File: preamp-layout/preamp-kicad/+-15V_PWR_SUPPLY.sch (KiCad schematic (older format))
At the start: 33 parts, among them J10 Conn_01x03_Male, J11 Conn_01x03_Male, J8 Screw_Terminal_01x03, J9 Conn_01x03_Male, T1 Transformer_1P_2S, U1 LM7815, U2 LM7915

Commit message: Power Supply Update
Grounding made more clear, tied to chassis on AC board. Pins renamed. Aligned with AC wall power convention. General cleanup.
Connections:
- net labels added: AC_HOT, AC_N
- net labels removed: AC+, AC-
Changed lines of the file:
@@
 $EndDescr
 Text HLabel 1950 3250 1    50   UnSpc ~ 0
-AC+
+AC_HOT
 Text HLabel 1950 3650 3    50   UnSpc ~ 0
-AC-
+AC_N
 Text GLabel 3900 6000 1    50   UnSpc ~ 0
 +15V

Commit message: RefDes Update
Re-ran refdes assignment, updated BOM accordingly.
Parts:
- renumbered J11 to J10, J8 to J7, J9 to J8, J10 to J9
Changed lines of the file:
@@
 	4150 3450 4150 4050
 $Comp
-L Connector:Conn_01x03_Male J9
+L Connector:Conn_01x03_Male J8
 U 1 1 5E5A9FCF
 P 3100 5800
-AR Path="/5E27B612/5E5A9FCF" Ref="J9"  Part="1"
+AR Path="/5E27B612/5E5A9FCF" Ref="J8"  Part="1"
 AR Path="/6009D432/5E5A9FCF" Ref="J?"  Part="1"
 AR Path="/5E1A0CE1/5E5A9FCF" Ref="J?"  Part="1"
-F 0 "J9" H 3072 5778 50  0000 R CNN
+F 0 "J8" H 3072 5778 50  0000 R CNN
 F 1 "Conn_01x03_Male" H 3072 5733 50  0001 R CNN
 F 2 "Connector_JST:JST_EH_B3B-EH-A_1x03_P2.50mm_Vertical" H 3100 5800 50  0001 C CNN
@@
 $EndComp
 $Comp
-L Connector:Conn_01x03_Male J10
+L Connector:Conn_01x03_Male J9
 U 1 1 5E5BC88E
 P 3100 6400
-AR Path="/5E27B612/5E5BC88E" Ref="J10"  Part="1"
+AR Path="/5E27B612/5E5BC88E" Ref="J9"  Part="1"
 AR Path="/6009D432/5E5BC88E" Ref="J?"  Part="1"
 AR Path="/5E1A0CE1/5E5BC88E" Ref="J?"  Part="1"
-F 0 "J10" H 3072 6378 50  0000 R CNN
+F 0 "J9" H 3072 6378 50  0000 R CNN
 F 1 "Conn_01x03_Male" H 3072 6333 50  0001 R CNN
 F 2 "Connector_JST:JST_EH_B3B-EH-A_1x03_P2.50mm_Vertical" H 3100 6400 50  0001 C CNN
@@
 $EndComp
 $Comp
-L Connector:Conn_01x03_Male J11
+L Connector:Conn_01x03_Male J10
 U 1 1 5E5C1243
 P 3100 7000
-AR Path="/5E27B612/5E5C1243" Ref="J11"  Part="1"
+AR Path="/5E27B612/5E5C1243" Ref="J10"  Part="1"
 AR Path="/6009D432/5E5C1243" Ref="J?"  Part="1"
 AR Path="/5E1A0CE1/5E5C1243" Ref="J?"  Part="1"
-F 0 "J11" H 3072 6978 50  0000 R CNN
+F 0 "J10" H 3072 6978 50  0000 R CNN
 F 1 "Conn_01x03_Male" H 3072 6933 50  0001 R CNN
 F 2 "Connector_JST:JST_EH_B3B-EH-A_1x03_P2.50mm_Vertical" H 3100 7000 50  0001 C CNN
@@
 AR Path="/5E26F6FE/5E8FCAF8" Ref="J?"  Part="1"
 AR Path="/5E5EF2D4/5E8FCAF8" Ref="J?"  Part="1"
-AR Path="/5E27B612/5E8FCAF8" Ref="J8"  Part="1"
-F 0 "J8" H 1268 3675 50  0000 C CNN
+AR Path="/5E27B612/5E8FCAF8" Ref="J7"  Part="1"
+F 0 "J7" H 1268 3675 50  0000 C CNN
 F 1 "Screw_Terminal_01x03" H 1268 3216 50  0001 C CNN
 F 2 "TerminalBlock_Phoenix:TerminalBlock_Phoenix_MKDS-3-3-5.08_1x03_P5.08mm_Horizontal" H 1350 3450 50  0001 C CNN

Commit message: Prelim PCB layout
Work done to lay out PCBs. Saving in anticipation of creating branch with a different input switching topology.
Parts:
- removed RV1, RV2: 5k, symbol Device:R_POT_US
- removed U1: LM7815, Package_TO_SOT_THT:TO-220-3_Vertical, symbol Regulator_Linear:L7805
- removed U2: LM7915, Package_TO_SOT_THT:TO-220-3_Vertical, symbol Regulator_Linear:LM7905_TO220
- added RV1, RV2: 4.7k, Potentiometer_THT:Potentiometer_Bourns_3386P_Vertical, symbol Device:R_POT
- added U1: LM7815, Package_TO_SOT_THT:TO-220-3_Vertical, symbol Regulator_Linear:LM7815_TO220
- added U2: LM7915, Package_TO_SOT_THT:TO-220-3_Vertical, symbol Regulator_Linear:LM7915_TO220
- F2: footprint (none) -> preamp:01110501Z_3AG
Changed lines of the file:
@@
 F 0 "F2" V 2053 3350 50  0000 C CNN
 F 1 "500mA" V 2144 3350 50  0000 C CNN
-F 2 "" V 2180 3350 50  0001 C CNN
+F 2 "preamp:01110501Z_3AG" V 2180 3350 50  0001 C CNN
 F 3 "~" H 2250 3350 50  0001 C CNN
 	1    2250 3350
@@
 	1    0    0    -1
 $EndComp
-Text Label 3550 4050 3    50   ~ 0
+Text Label 3550 4000 3    50   ~ 0
 rectified_-
-Text Label 4150 4050 3    50   ~ 0
+Text Label 4150 4000 3    50   ~ 0
 rectified_+
 $Comp
@@
 Text Label 5500 2350 2    50   ~ 0
 rectified_+
-$Comp
-L Regulator_Linear:L7805 U?
-U 1 1 5FE3F8F2
-P 7800 2350
-AR Path="/5E5EF2D4/5FE3F8F2" Ref="U?"  Part="1"
-AR Path="/5E27B612/5FE3F8F2" Ref="U1"  Part="1"
-F 0 "U1" H 7800 2592 50  0000 C CNN
-F 1 "LM7815" H 7800 2501 50  0000 C CNN
-F 2 "Package_TO_SOT_THT:TO-220-3_Vertical" H 7825 2200 50  0001 L CIN
-F 3 "http://www.st.com/content/ccc/resource/technical/document/datasheet/41/4f/b3/b0/12/d4/47/88/CD00000444.pdf/files/CD00000444.pdf/jcr:content/translations/en.CD00000444.pdf" H 7800 2300 50  0001 C CNN
-	1    7800 2350
-	1    0    0    -1
-$EndComp
 Connection ~ 5700 3550
-$Comp
-L Regulator_Linear:LM7905_TO220 U?
-U 1 1 5FE3F8FA
-P 7800 4750
-AR Path="/5E5EF2D4/5FE3F8FA" Ref="U?"  Part="1"
-AR Path="/5E27B612/5FE3F8FA" Ref="U2"  Part="1"
-F 0 "U2" H 7800 4601 50  0000 C CNN
-F 1 "LM7915" H 7800 4510 50  0000 C CNN
-F 2 "Package_TO_SOT_THT:TO-220-3_Vertical" H 7800 4550 50  0001 C CIN
-F 3 "http://www.fairchildsemi.com/ds/LM/LM7905.pdf" H 7800 4750 50  0001 C CNN
-	1    7800 4750
-	1    0    0    -1
-$EndComp
-$Comp
-L Device:R_POT_US RV?
-U 1 1 5FE3F900
-P 7800 3250
-AR Path="/5E5EF2D4/5FE3F900" Ref="RV?"  Part="1"
-AR Path="/5E27B612/5FE3F900" Ref="RV1"  Part="1"
-F 0 "RV1" H 7732 3296 50  0000 R CNN
-F 1 "5k" H 7732 3205 50  0000 R CNN
-F 2 "" H 7800 3250 50  0001 C CNN
-F 3 "~" H 7800 3250 50  0001 C CNN
-	1    7800 3250
-	1    0    0    -1
-$EndComp
 Wire Wire Line
 	7950 3250 8050 3250
@@
 Text GLabel 9900 5000 3    50   UnSpc ~ 0
 -15V
-$Comp
-L Device:R_POT_US RV?
-U 1 1 5FE3F975
-P 7800 3850
-AR Path="/5E5EF2D4/5FE3F975" Ref="RV?"  Part="1"
-AR Path="/5E27B612/5FE3F975" Ref="RV2"  Part="1"
-F 0 "RV2" H 7732 3804 50  0000 R CNN
-F 1 "5k" H 7732 3895 50  0000 R CNN
-F 2 "" H 7800 3850 50  0001 C CNN
-F 3 "~" H 7800 3850 50  0001 C CNN
-	1    7800 3850
-	1    0    0    1
-$EndComp
 Wire Wire Line
 	7950 3850 8050 3850
@@
 Wire Wire Line
 	3300 3850 3850 3850
-Wire Wire Line
-	3550 4050 3550 3450
-Wire Wire Line
-	4150 3450 4150 4050
 $Comp
 L Connector:Conn_01x03_Male J8
@@
 Wire Wire Line
 	9900 4750 9900 5000
+$Comp
+L Regulator_Linear:LM7815_TO220 U1
+U 1 1 612FF6B0
+P 7800 2350
+F 0 "U1" H 7800 2592 50  0000 C CNN
+F 1 "LM7815" H 7800 2501 50  0000 C CNN
+F 2 "Package_TO_SOT_THT:TO-220-3_Vertical" H 7800 2575 50  0001 C CIN
+F 3 "http://www.fairchildsemi.com/ds/LM/LM7805.pdf" H 7800 2300 50  0001 C CNN
+	1    7800 2350
+	1    0    0    -1
+$EndComp
+$Comp
+L Regulator_Linear:LM7915_TO220 U2
+U 1 1 6130D110
+P 7800 4750
+F 0 "U2" H 7800 4601 50  0000 C CNN
+F 1 "LM7915" H 7800 4510 50  0000 C CNN
+F 2 "Package_TO_SOT_THT:TO-220-3_Vertical" H 7800 4550 50  0001 C CIN
+F 3 "http://www.fairchildsemi.com/ds/LM/LM7905.pdf" H 7800 4750 50  0001 C CNN
+	1    7800 4750
+	1    0    0    -1
+$EndComp
+$Comp
+L Device:R_POT RV?
+U 1 1 613227DC
+P 7800 3250
+AR Path="/5E5EF2D4/613227DC" Ref="RV?"  Part="1"
+AR Path="/5E27B612/613227DC" Ref="RV1"  Part="1"
+F 0 "RV1" H 7730 3296 50  0000 R CNN
+F 1 "4.7k" H 7730 3205 50  0000 R CNN
+F 2 "Potentiometer_THT:Potentiometer_Bourns_3386P_Vertical" H 7800 3250 50  0001 C CNN
+F 3 "~" H 7800 3250 50  0001 C CNN
+	1    7800 3250
+	1    0    0    -1
+$EndComp
+$Comp
+L Device:R_POT RV?
+U 1 1 61335892
+P 7800 3850
+AR Path="/5E5EF2D4/61335892" Ref="RV?"  Part="1"
+AR Path="/5E27B612/61335892" Ref="RV2"  Part="1"
+F 0 "RV2" H 7730 3896 50  0000 R CNN
+F 1 "4.7k" H 7730 3805 50  0000 R CNN
+F 2 "Potentiometer_THT:Potentiometer_Bourns_3386P_Vertical" H 7800 3850 50  0001 C CNN
+F 3 "~" H 7800 3850 50  0001 C CNN
+	1    7800 3850
+	1    0    0    -1
+$EndComp
+Wire Wire Line
+	3550 3450 3550 4000
+Wire Wire Line
+	4150 3450 4150 4000
 $EndSCHEMATC

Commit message: Periodic backup
Extensive changes as a result of PCB layout phase.
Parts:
- T1: footprint (none) -> preamp:164J28
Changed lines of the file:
@@
 F 0 "T1" H 2900 3939 50  0000 C CNN
 F 1 "Transformer_1P_2S" H 2900 3940 50  0001 C CNN
-F 2 "" H 2900 3450 50  0001 C CNN
+F 2 "preamp:164J28" H 2900 3450 50  0001 C CNN
 F 3 "~" H 2900 3450 50  0001 C CNN
 	1    2900 3450

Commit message: PCB layout
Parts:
- removed C10, C11: 100uF, Capacitor_THT:CP_Radial_D6.3mm_P2.50mm, symbol Device:CP1
- removed C2, C3, C4, C5: 2200uF, Capacitor_THT:CP_Radial_D12.5mm_P5.00mm, symbol Device:CP1
- removed C6, C7, C8, C9: 0.1uF, Capacitor_SMD:C_0805_2012Metric_Pad1.15x1.40mm_HandSolder, symbol Device:C
- removed D1: DF02M, Diode_THT:Diode_Bridge_DIP-4_W7.62mm_P5.08mm, symbol Diode_Bridge:DF02M
- removed D4, D5, D6, D7: SM4001, Diode_SMD:D_SOD-123F, symbol Device:D
- removed R4, R5: 10R 1W, Resistor_THT:R_Axial_DIN0414_L11.9mm_D4.5mm_P15.24mm_Horizontal, symbol Device:R
- removed R6, R7: 240R, Resistor_SMD:R_1206_3216Metric_Pad1.42x1.75mm_HandSolder, symbol Device:R
- removed RV1, RV2: 4.7k, Potentiometer_THT:Potentiometer_Bourns_3386P_Vertical, symbol Device:R_POT
- removed T1: Transformer_1P_2S, preamp:164J28, symbol Device:Transformer_1P_2S
- removed U1: LM7815, Package_TO_SOT_THT:TO-220-3_Vertical, symbol Regulator_Linear:LM7815_TO220
- removed U2: LM7915, Package_TO_SOT_THT:TO-220-3_Vertical, symbol Regulator_Linear:LM7915_TO220
- added PS1, PS2: IRM-10-15, Converter_ACDC:Converter_ACDC_MeanWell_IRM-10-xx_THT, symbol Converter_ACDC:IRM-10-15
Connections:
- net +15V: now also PS1.4 (+Vo)
- net -15V: now also PS2.3 (-Vo)
- net AC_N: now also PS1.1 (AC/N), PS2.1 (AC/N)
- net GND: now also PS1.3 (-Vo), PS2.4 (+Vo)
- net at F2.1: now also PS1.2 (AC/L), PS2.2 (AC/L)
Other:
- note removed: "+19.2VDC"
- note removed: "-19.2VDC"
- note removed: "28VAC"
- moved on the sheet: F2, J7

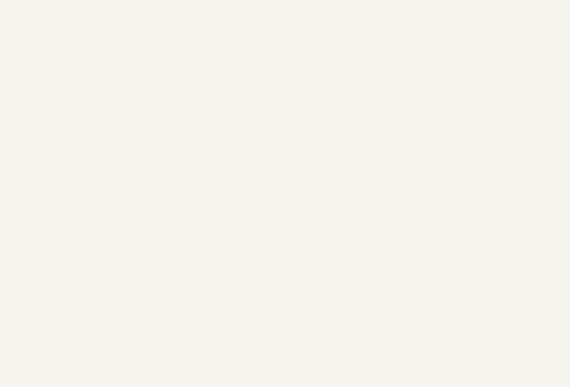
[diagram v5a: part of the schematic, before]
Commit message: PCB layout update, front panel and LED restructure
Restructure of capacitive buttons. Restructure of MCU schematic. Moved LEDs to front panel sheet. Front panel and MCU initial PCB layout. 8 bit DAC update (grounded address pins). DAC connection renaming. Added mounting holes for boards.
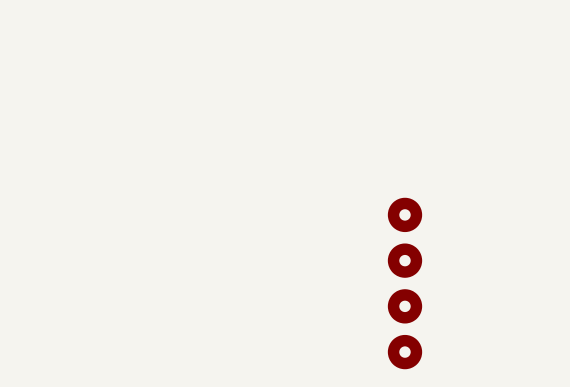
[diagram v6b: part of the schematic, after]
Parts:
- added H10, H11, H12, H9: MountingHole, MountingHole:MountingHole_3.2mm_M3, symbol Mechanical:MountingHole
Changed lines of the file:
@@
 Wire Wire Line
 	6850 3600 6850 3850
+$Comp
+L Mechanical:MountingHole H?
+U 1 1 5EE31613
+P 6750 6850
+AR Path="/5EE31613" Ref="H?"  Part="1"
+AR Path="/5E2D8DA2/5EE31613" Ref="H?"  Part="1"
+AR Path="/5E27B612/5EE31613" Ref="H9"  Part="1"
+F 0 "H9" H 6850 6850 50  0001 L CNN
+F 1 "MountingHole" H 6850 6805 50  0001 L CNN
+F 2 "MountingHole:MountingHole_3.2mm_M3" H 6750 6850 50  0001 C CNN
+F 3 "~" H 6750 6850 50  0001 C CNN
+	1    6750 6850
+	1    0    0    -1
+$EndComp
+$Comp
+L Mechanical:MountingHole H?
+U 1 1 5EE31619
+P 6750 7050
+AR Path="/5EE31619" Ref="H?"  Part="1"
+AR Path="/5E2D8DA2/5EE31619" Ref="H?"  Part="1"
+AR Path="/5E27B612/5EE31619" Ref="H10"  Part="1"
+F 0 "H10" H 6850 7050 50  0001 L CNN
+F 1 "MountingHole" H 6850 7005 50  0001 L CNN
+F 2 "MountingHole:MountingHole_3.2mm_M3" H 6750 7050 50  0001 C CNN
+F 3 "~" H 6750 7050 50  0001 C CNN
+	1    6750 7050
+	1    0    0    -1
+$EndComp
+$Comp
+L Mechanical:MountingHole H?
+U 1 1 5EE3161F
+P 6750 7250
+AR Path="/5EE3161F" Ref="H?"  Part="1"
+AR Path="/5E2D8DA2/5EE3161F" Ref="H?"  Part="1"
+AR Path="/5E27B612/5EE3161F" Ref="H11"  Part="1"
+F 0 "H11" H 6850 7250 50  0001 L CNN
+F 1 "MountingHole" H 6850 7205 50  0001 L CNN
+F 2 "MountingHole:MountingHole_3.2mm_M3" H 6750 7250 50  0001 C CNN
+F 3 "~" H 6750 7250 50  0001 C CNN
+	1    6750 7250
+	1    0    0    -1
+$EndComp
+$Comp
+L Mechanical:MountingHole H?
+U 1 1 5EE31625
+P 6750 7450
+AR Path="/5EE31625" Ref="H?"  Part="1"
+AR Path="/5E2D8DA2/5EE31625" Ref="H?"  Part="1"
+AR Path="/5E27B612/5EE31625" Ref="H12"  Part="1"
+F 0 "H12" H 6850 7450 50  0001 L CNN
+F 1 "MountingHole" H 6850 7405 50  0001 L CNN
+F 2 "MountingHole:MountingHole_3.2mm_M3" H 6750 7450 50  0001 C CNN
+F 3 "~" H 6750 7450 50  0001 C CNN
+	1    6750 7450
+	1    0    0    -1
+$EndComp
 $EndSCHEMATC
